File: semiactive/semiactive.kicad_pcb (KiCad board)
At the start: 2 copper layers, 85 x 85 mm, 12 parts, among them J1 5223004-2, U1 Teensy4.1

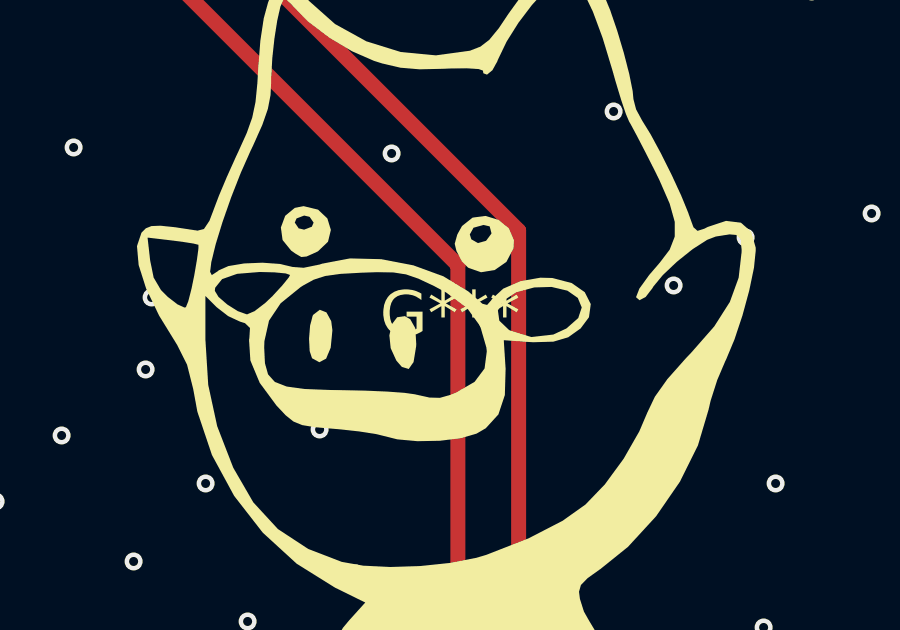
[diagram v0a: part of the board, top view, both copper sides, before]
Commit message: Critical ESPdaq fix
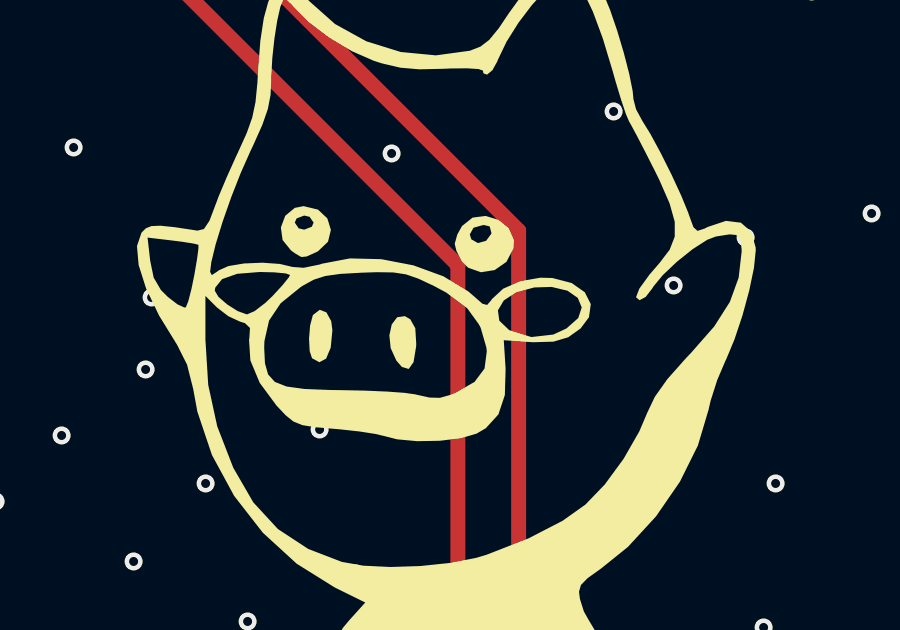
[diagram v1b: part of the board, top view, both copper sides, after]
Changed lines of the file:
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@@
     (at 182.118 82.296)
     (attr board_only exclude_from_pos_files exclude_from_bom)
-    (fp_text reference "G***" (at 0 0) (layer "F.SilkS")
+    (fp_text reference "G***" (at 0 0) (layer "F.SilkS") hide
         (effects (font (size 1.5 1.5) (thickness 0.3)))
     )

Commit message: BOM
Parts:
- added D7: D, Diode_SMD:D_SMA, F.Cu at (164.5, 46.0)
- C1, C2, C3: value C -> 1uF
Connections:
- U1 pad 48: 5V -> Net-(D7-A)
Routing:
- net 5V: track 175.3 -> 169.1 mm, vias 2 -> 3
- net Net-(D7-A): track 0.00 -> 3.63 mm

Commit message: Quote update
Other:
- board text added: "{dblquote}Andrew has very squeezable boobs{dblquote} - @Joe Keenan"
- board text added: "{dblquote}It's OK, I did the FEA in my head and it's all blue{dblquote} - @Ben"
- board text removed: "{dblquote}Andrew has very squeezable boobs{dblquote} @Joe Keenan"
- board text removed: "{dblquote}The best way to improve our team's performance is illegal drugs{dblquote} - @Ben"
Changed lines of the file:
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@@
     (effects (font (size 1 1) (thickness 0.15)) (justify left bottom mirror))
   )
-  (gr_text "{dblquote}Andrew has very squeezable boobs{dblquote} \n@Joe Keenan" (at 196.596 75.438) (layer "B.SilkS")
+  (gr_text "{dblquote}Andrew has very squeezable boobs{dblquote} \n- @Joe Keenan" (at 196.596 75.438) (layer "B.SilkS")
     (effects (font (size 1 1) (thickness 0.15)) (justify left bottom mirror))
   )
@@
     (effects (font (size 1 1) (thickness 0.15)) (justify left bottom mirror))
   )
-  (gr_text "{dblquote}The best way to improve our team's \nperformance is illegal drugs{dblquote} \n- @Ben" (at 146.812 117.602) (layer "B.SilkS")
+  (gr_text "{dblquote}It's OK, I did the FEA in my \nhead and it's all blue{dblquote}\n- @Ben" (at 146.812 117.602) (layer "B.SilkS")
     (effects (font (size 1 1) (thickness 0.15)) (justify left bottom mirror))
   )
